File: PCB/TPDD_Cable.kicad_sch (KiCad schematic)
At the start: 11 parts, among them J2 TPDD, P2 RX, P20 DSR, P3 TX, P4 CTS, P5 RTS, P6 DTR, P7 GND, Q1 DTA114EKA, Q2 DTA114EKA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

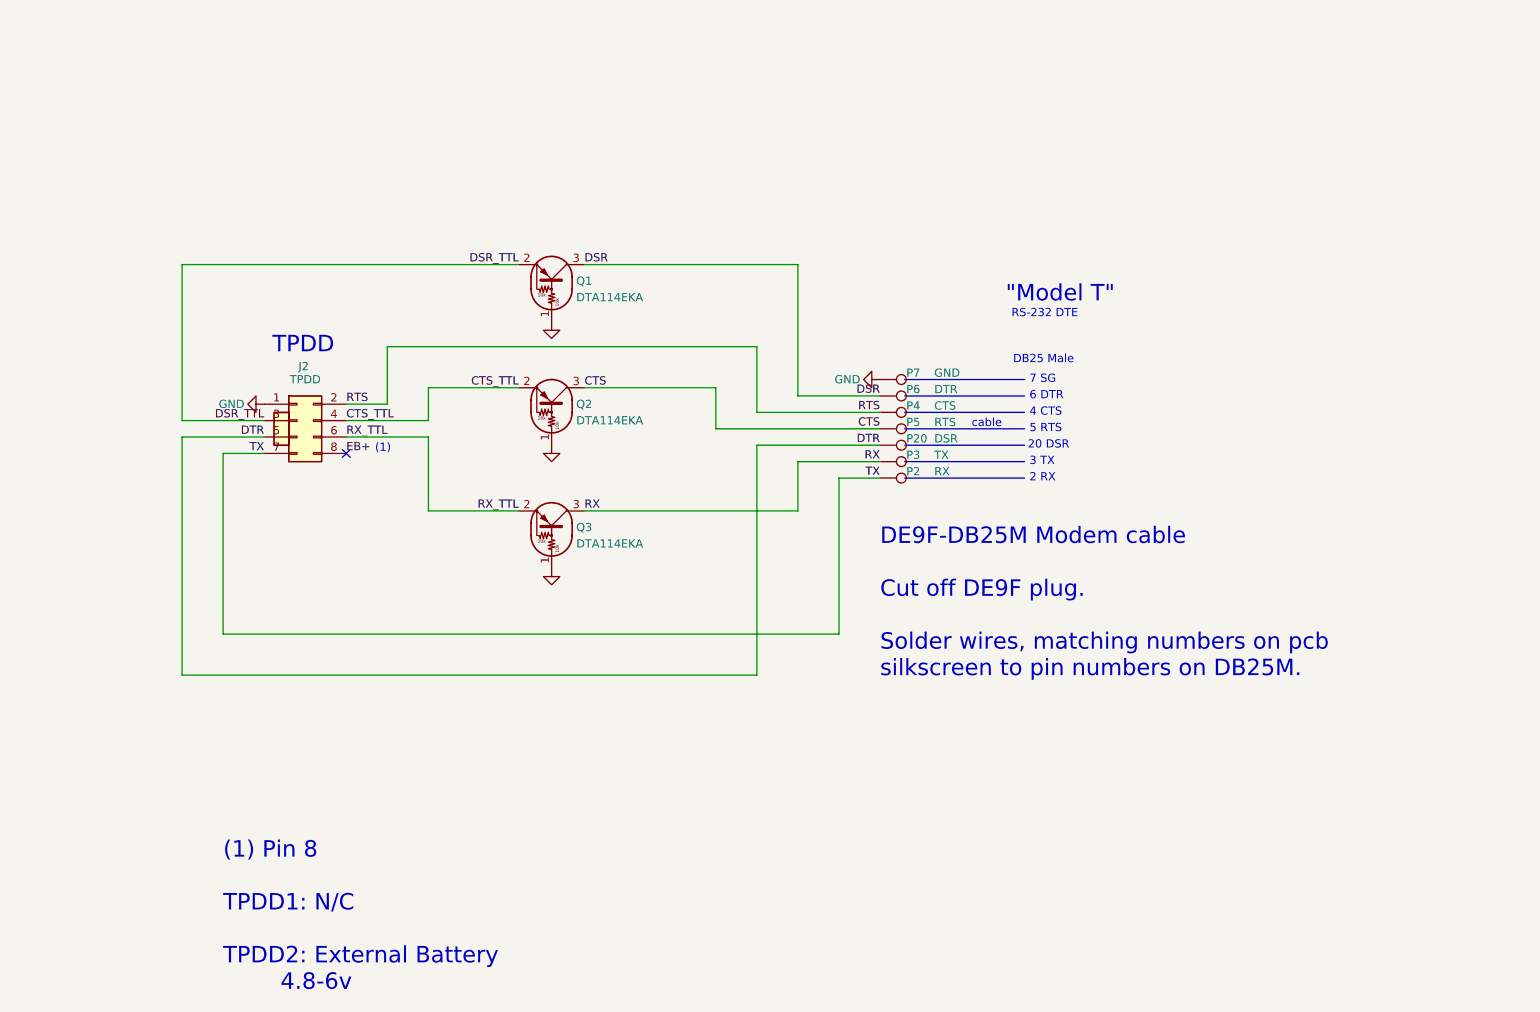
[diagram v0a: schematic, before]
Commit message: pcb 2 is new default, smt wire pads
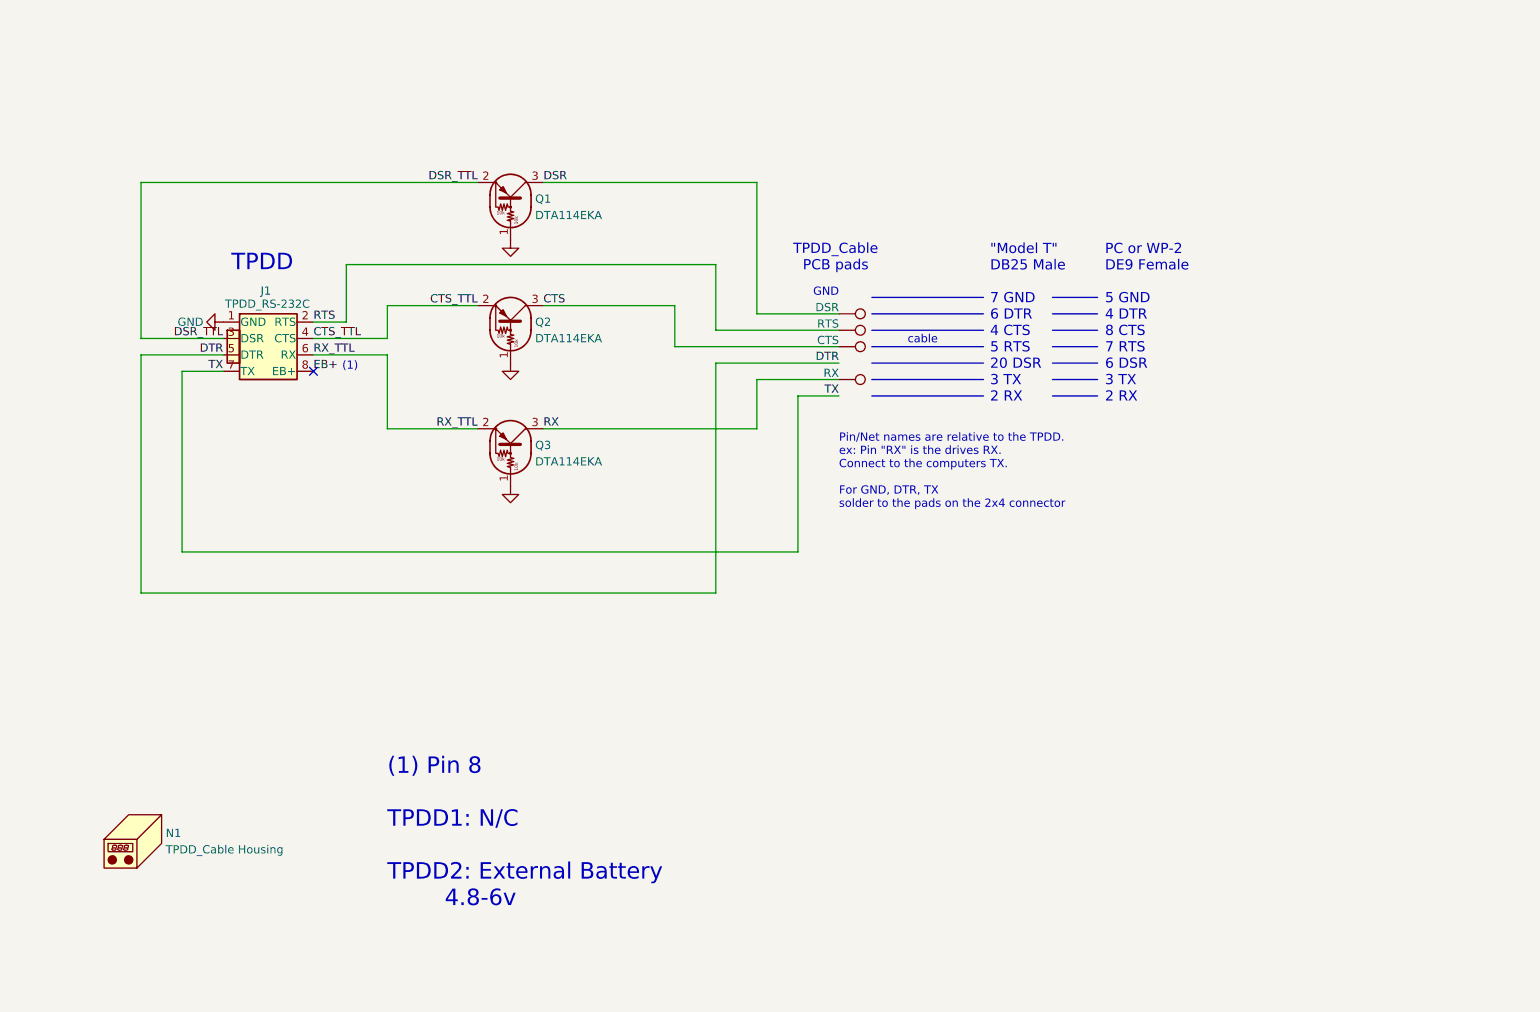
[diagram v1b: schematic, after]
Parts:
- removed J2: TPDD, 000_LOCAL:2x4x2.54mm_edge_mount, symbol 000_LOCAL:Conn_02x04_Odd_Even
- removed P2: RX, 000_LOCAL:PTH_0.65x1.2, symbol 000_LOCAL:TestPoint
- removed P20: DSR, 000_LOCAL:PTH_0.65x1.2, symbol 000_LOCAL:TestPoint
- removed P7: GND, 000_LOCAL:PTH_0.65x1.2, symbol 000_LOCAL:TestPoint
- added J1: TPDD_RS-232C, 000_LOCAL:2x4x2.54mm_edge_mount, symbol 000_LOCAL:TPDD_RS-232C
- added N1: TPDD_Cable Housing, 000_LOCAL:TPDD_Cable_Housing, symbol 000_LOCAL:Housing
- P3: value TX -> RX; footprint 000_LOCAL:PTH_0.65x1.2 -> 000_LOCAL:SMD_1.2x3
- P4: value CTS -> RTS; footprint 000_LOCAL:PTH_0.65x1.2 -> 000_LOCAL:SMD_1.2x3
- P5: value RTS -> CTS; footprint 000_LOCAL:PTH_0.65x1.2 -> 000_LOCAL:SMD_1.2x3
- P6: value DTR -> DSR; footprint 000_LOCAL:PTH_0.65x1.2 -> 000_LOCAL:SMD_1.2x3
- Q1, Q2, Q3: MPN (none) -> DTA114EKA
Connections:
- net CTS_TTL: now also J1.4 (CTS)
- net DSR_TTL: now also J1.3 (DSR)
- net DTR: now also J1.5 (DTR)
- net EB+: now also J1.8 (EB+)
- net GND: now also J1.1 (GND)
- net RTS: now also J1.2 (RTS)
- net RX_TTL: now also J1.6 (RX)
- net TX: now also J1.7 (TX)
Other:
- note added: ""Model T" DB25 Male 7 GND 6 DTR 4 CTS 5 RTS 20 DSR 3 TX 2 RX"
- note added: "GND"
- note added: "PC or WP-2 DE9 Female 5 GND 4 DTR 8 CTS 7 RTS 6 DSR 3 TX 2 RX"
- note added: "Pin/Net names are relative to the TPDD. ex: Pin "RX" is the drives RX. Connect to the computers TX. For GND, DTR, TX solder to the pads on the 2x4 connector"
- note added: "TPDD_Cable PCB pads"
- note removed: ""Model T""
- note removed: "2 RX"
- note removed: "20 DSR"
- note removed: "3 TX"
- note removed: "4 CTS"
- note removed: "5 RTS"
- note removed: "6 DTR"
- note removed: "7 SG"
- note removed: "DB25 Male"
- note removed: "DE9F-DB25M Modem cable Cut off DE9F plug. Solder wires, matching numbers on pcb silkscreen to pin numbers on DB25M."
- note removed: "RS-232 DTE"
- moved on the sheet: Q1, Q2, Q3

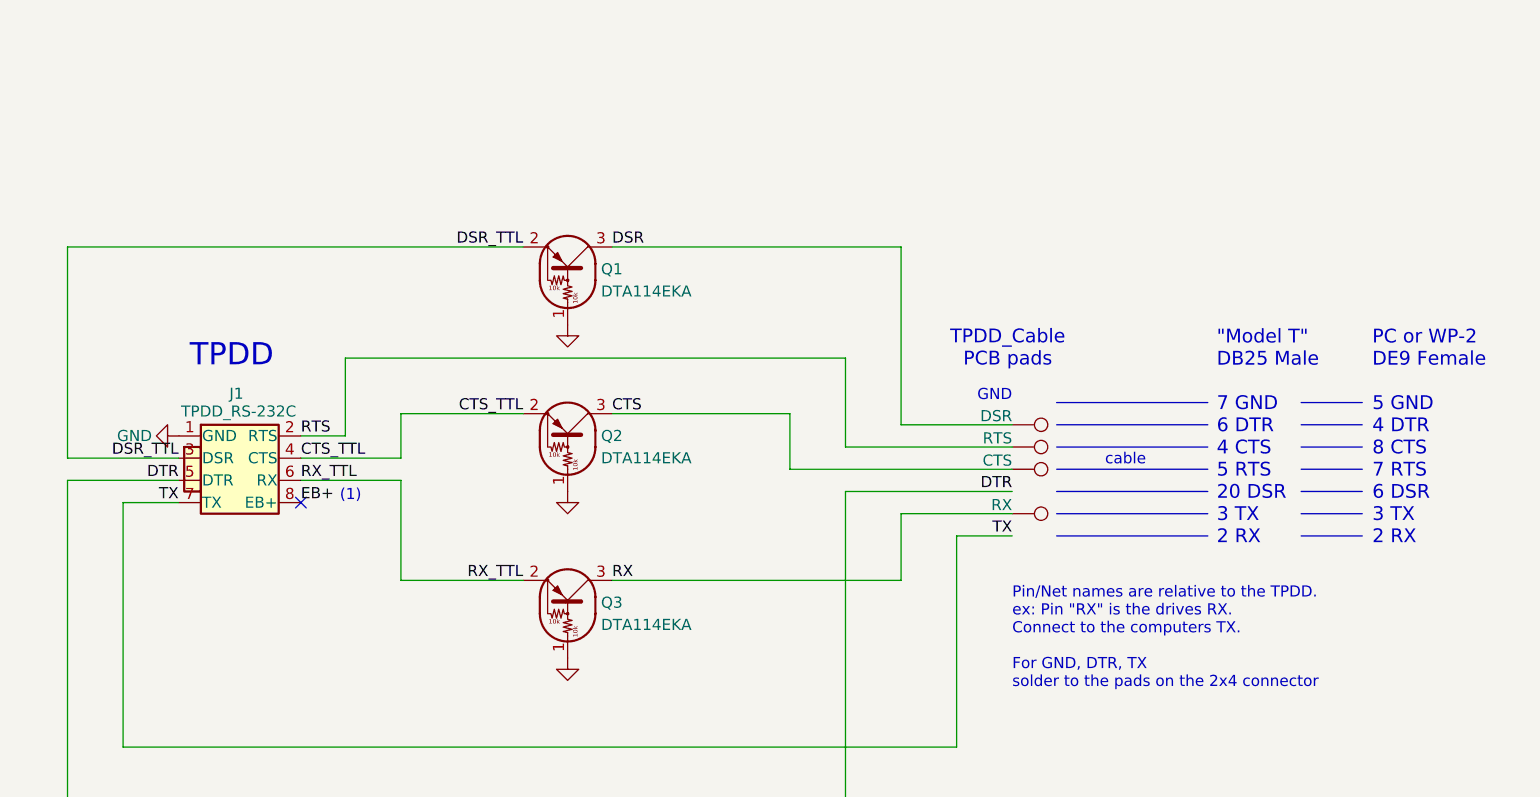
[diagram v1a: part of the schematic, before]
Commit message: correct DTE vs DCE signal names & DE9 pinout in schematic
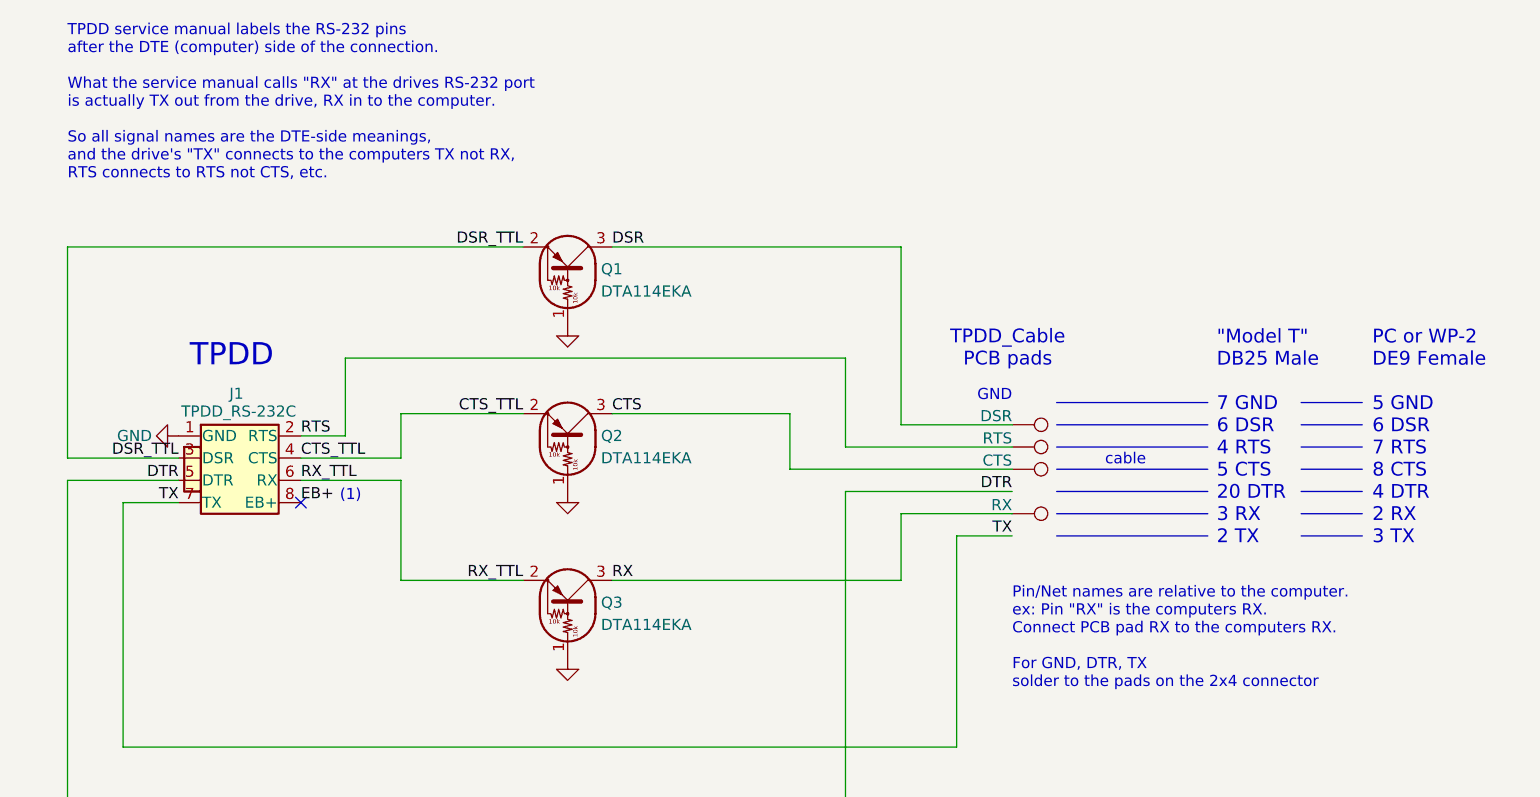
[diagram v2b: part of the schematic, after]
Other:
- note added: ""Model T" DB25 Male 7 GND 6 DSR 4 RTS 5 CTS 20 DTR 3 RX 2 TX"
- note added: "PC or WP-2 DE9 Female 5 GND 6 DSR 7 RTS 8 CTS 4 DTR 2 RX 3 TX"
- note added: "Pin/Net names are relative to the computer. ex: Pin "RX" is the computers RX. Connect PCB pad RX to the computers RX. For GND, DTR, TX solder to the pads on the 2x4 connector"
- note added: "TPDD service manual labels the RS-232 pins after the DTE (computer) side of the connection. What the service manual calls "RX" at the drives RS-232 port is actually TX out from the drive, RX in to the computer. So all signal names are the DTE-side meanings, and the drive's "TX" connects to the computers TX not RX, RTS connects to RTS not CTS, etc."
- note removed: ""Model T" DB25 Male 7 GND 6 DTR 4 CTS 5 RTS 20 DSR 3 TX 2 RX"
- note removed: "PC or WP-2 DE9 Female 5 GND 4 DTR 8 CTS 7 RTS 6 DSR 3 TX 2 RX"
- note removed: "Pin/Net names are relative to the TPDD. ex: Pin "RX" is the drives RX. Connect to the computers TX. For GND, DTR, TX solder to the pads on the 2x4 connector"
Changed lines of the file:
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@@
 	(title_block
 		(title "TPDD-RS-232")
-		(date "2024-10-10")
-		(rev "4")
+		(date "2024-10-23")
+		(rev "5")
 		(company "Brian K. White")
 	)
@@
 		)
 	)
-	(text "Pin/Net names are relative to the TPDD.\nex: Pin \"RX\" is the drives RX.\nConnect to the computers TX.\n\nFor GND, DTR, TX\nsolder to the pads on the 2x4 connector\n"
+	(text "TPDD service manual labels the RS-232 pins\nafter the DTE (computer) side of the connection.\n\nWhat the service manual calls \"RX\" at the drives RS-232 port\nis actually TX out from the drive, RX in to the computer.\n\nSo all signal names are the DTE-side meanings,\nand the drive's \"TX\" connects to the computers TX not RX,\nRTS connects to RTS not CTS, etc.\n"
+		(exclude_from_sim no)
+		(at 63.5 38.1 0)
+		(effects
+			(font
+				(size 1.27 1.27)
+			)
+			(justify left top)
+		)
+	)
+	(text "Pin/Net names are relative to the computer.\nex: Pin \"RX\" is the computers RX.\nConnect PCB pad RX to the computers RX.\n\nFor GND, DTR, TX\nsolder to the pads on the 2x4 connector\n"
 		(exclude_from_sim no)
 		(at 171.45 102.362 0)
@@
 		)
 	)
-	(text "PC or WP-2\nDE9 Female\n\n5 GND\n4 DTR\n8 CTS\n7 RTS\n6 DSR\n3 TX\n2 RX"
+	(text "PC or WP-2\nDE9 Female\n\n5 GND\n6 DSR\n7 RTS\n8 CTS\n4 DTR\n2 RX\n3 TX"
 		(exclude_from_sim no)
 		(at 212.598 85.344 0)
@@
 		)
 	)
-	(text "\"Model T\"\nDB25 Male\n\n7 GND\n6 DTR\n4 CTS\n5 RTS\n20 DSR\n3 TX\n2 RX"
+	(text "\"Model T\"\nDB25 Male\n\n7 GND\n6 DSR\n4 RTS\n5 CTS\n20 DTR\n3 RX\n2 TX"
 		(exclude_from_sim no)
 		(at 194.818 85.344 0)
